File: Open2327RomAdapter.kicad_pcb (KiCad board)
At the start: 2 copper layers, 19.6 x 41.5 mm, 7 parts, among them P1 Conn_01x04, P99 OSHW_LOGO, U1 2364, U2 27128

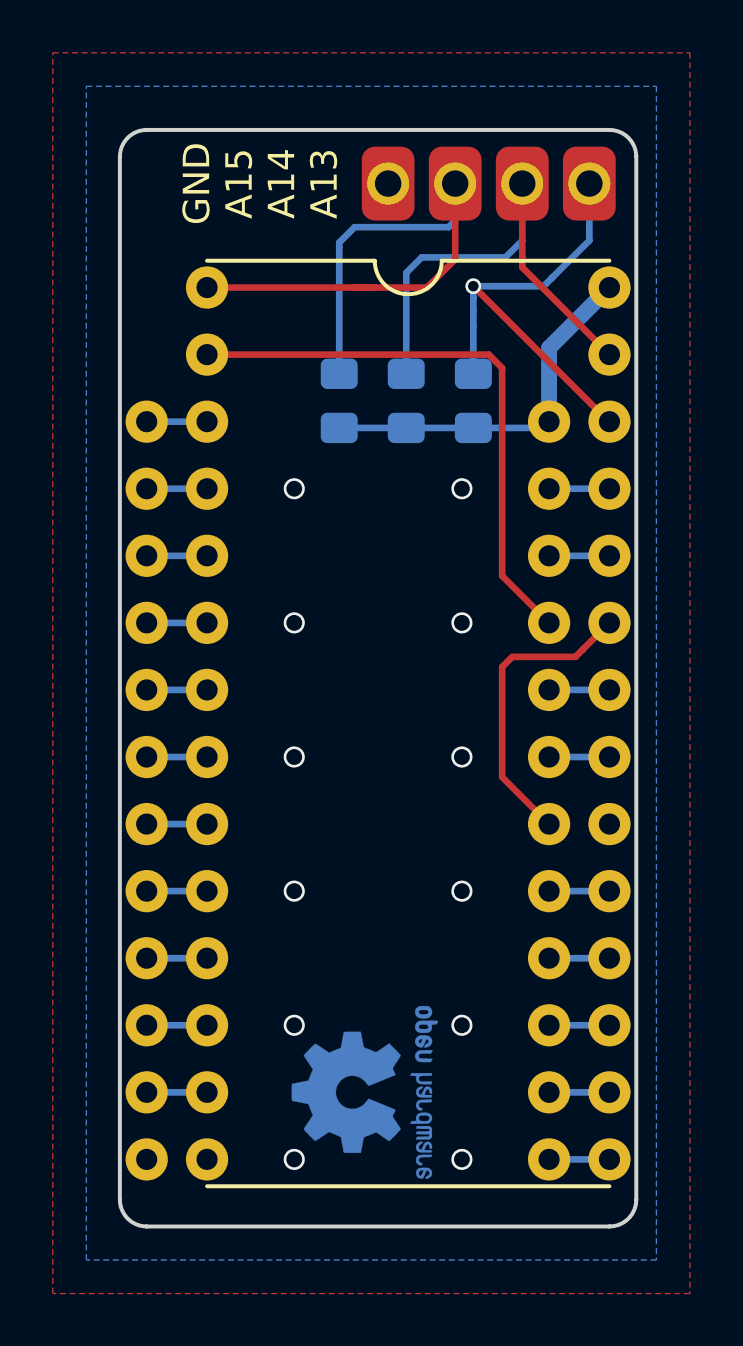
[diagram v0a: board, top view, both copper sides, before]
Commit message: Add jumper, pull-up and pad so that A12 can optionally be driven externally
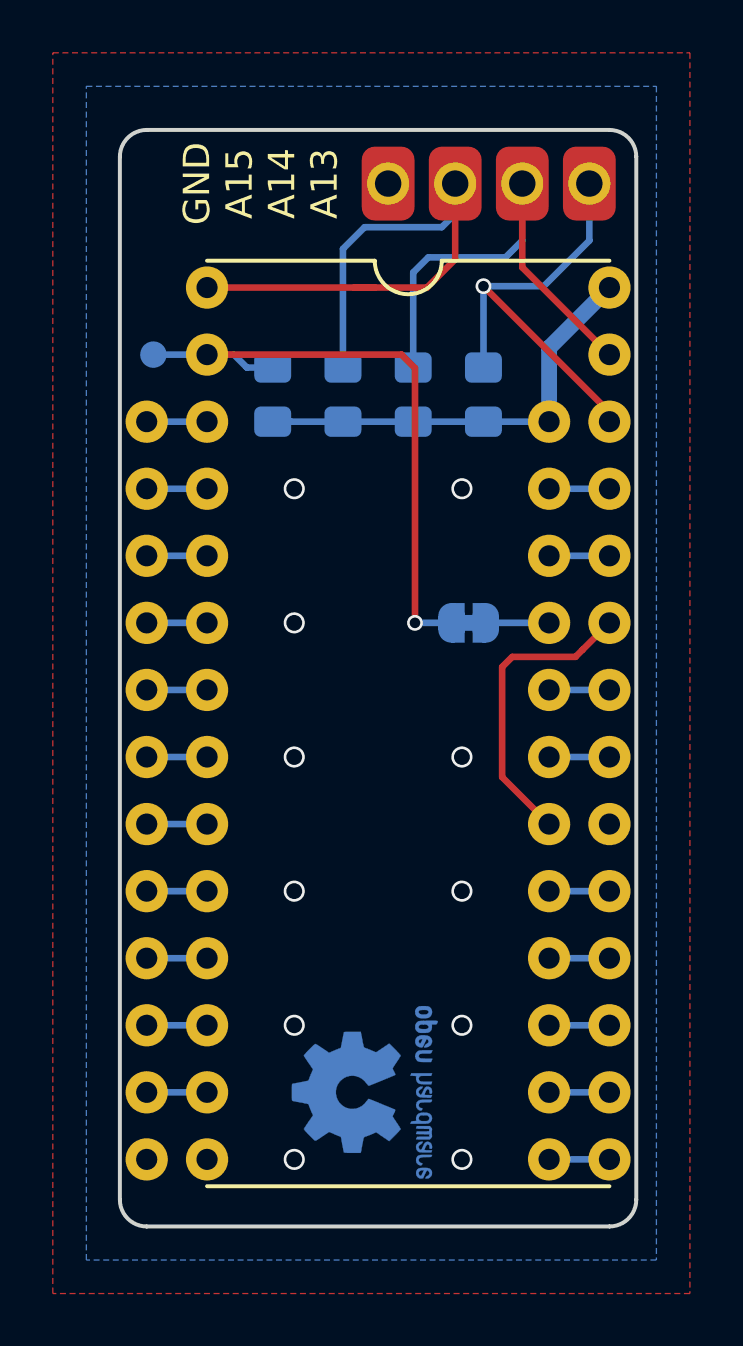
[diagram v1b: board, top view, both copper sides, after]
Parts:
- added J1: CONN_A12, TestPoint:TestPoint_Pad_D1.0mm, B.Cu at (146.6, 104.1)
- added JP1: JUMPER_4K_SW, Jumper:SolderJumper-2_P1.3mm_Bridged_RoundedPad1.0x1.5mm, B.Cu at (158.5, 114.3)
- added R4: 10k, Resistor_SMD:R_0805_2012Metric_Pad1.15x1.40mm_HandSolder, B.Cu at (151.1, 105.7)
- U1: value 2364 -> 2364_SOCKET
- moved R1 0.45 mm to (159.1, 105.7)
- moved R2 0.35 mm to (156.4, 105.7)
- moved R3 0.28 mm to (153.7, 105.7)
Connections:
- U1 pad 21: Net-(U1-Pad21) -> Net-(JP1-Pad2)
- U2 pad 2: Net-(U1-Pad21) -> Net-(J1-Pad1)
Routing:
- net Net-(J1-Pad1): track 0.00 -> 24.1 mm, vias 0 -> 1
- net Net-(U1-Pad21): track 21.8 -> 0.00 mm
- net VCC: track 14.1 -> 16.5 mm
- net Net-(JP1-Pad2): track 0.00 -> 2.40 mm
- net Net-(P1-Pad4): track 17.9 -> 17.1 mm
- net Net-(P1-Pad2): track 24.6 -> 23.9 mm
- net GND: vias 12 -> 11
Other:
- board text added: "A12"
